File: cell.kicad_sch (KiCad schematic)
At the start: 6 parts, among them Q13 DMG2305UX-7

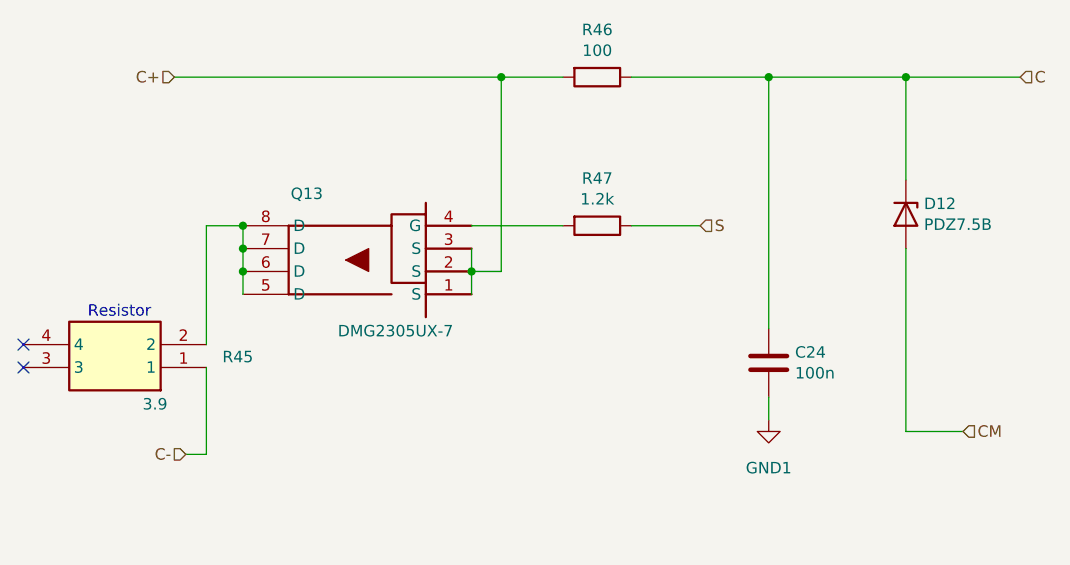
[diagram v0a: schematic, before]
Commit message: Replace broken 8-pin DMG2305UX symbol with correct 3-pin SamacSys version
- Updated lib_symbols with official DMG2305UX-7 symbol (G/S/D pins 1/2/3)
- Added SOT96P240X115-3N footprint file
- Applied to both cell.kicad_sch and cell2.kicad_sch

Note: Wire connections may need adjustment in KiCad GUI since pin geometry changed
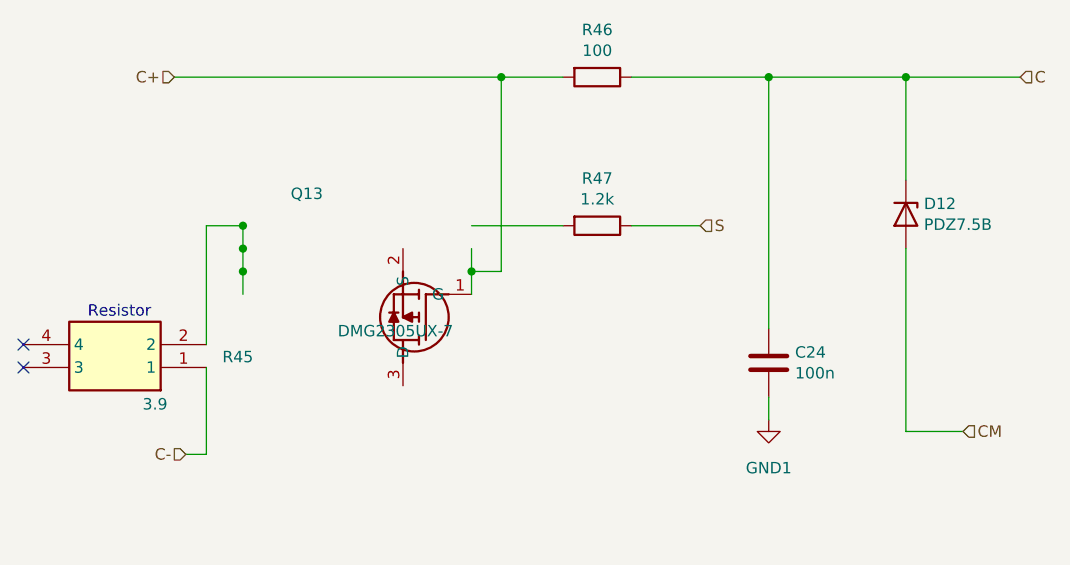
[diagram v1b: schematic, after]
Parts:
- Q13: symbol Custom:DMG2305UX -> Samacsys:DMG2305UX-7
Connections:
- net C+: no longer Q13.2 (S), Q13.3 (S)
- net at R47.2: no longer Q13.4 (G)
- now unconnected: R45.2
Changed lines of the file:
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@@
 	)
 	(symbol
-		(lib_id "Custom:DMG2305UX")
+		(lib_id "Samacsys:DMG2305UX-7")
 		(at 129.794 100.584 180)
 		(unit 1)

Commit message: Adjust balancing resistor and balancing mosfet
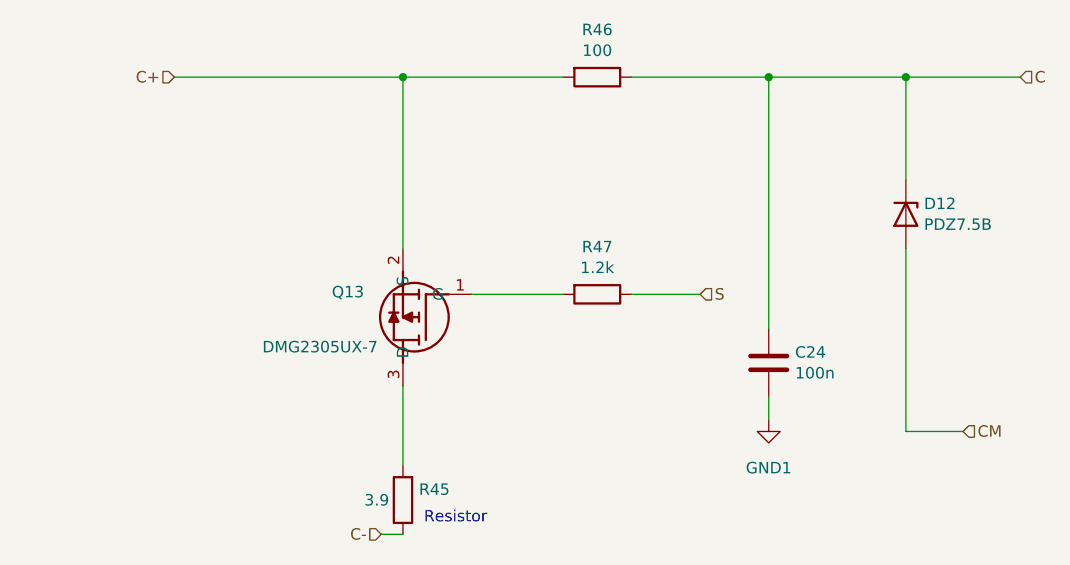
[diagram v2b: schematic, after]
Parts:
- R45: symbol Samacsys_kicad_sym:PWR263S-20-2R50J -> Device:R
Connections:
- net C+: now also Q13.2 (S); no longer Q13.1 (G)
- net at R47.2: now also Q13.1 (G)
- net at Q13.3 (D): now also R45.2
- no-connect marks 2 -> 0
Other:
- moved on the sheet: R47
